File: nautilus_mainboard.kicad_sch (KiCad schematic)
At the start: 0 parts

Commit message: added piezzo circuit and i2c line
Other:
- sheet STM ports: added Pack1_SCL, Pack1_SDA; removed none
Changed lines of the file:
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@@
+	(wire
+		(pts
+			(xy 184.15 93.98) (xy 184.15 90.17)
+		)
+		(stroke
+			(width 0)
+			(type default)
+		)
+	)
+	(wire
+		(pts
+			(xy 184.15 90.17) (xy 55.88 90.17)
+		)
+		(stroke
+			(width 0)
+			(type default)
+		)
+	)
 	(wire
 		(pts
@@
 	(wire
 		(pts
+			(xy 186.69 87.63) (xy 59.69 87.63)
+		)
+		(stroke
+			(width 0)
+			(type default)
+		)
+	)
+	(wire
+		(pts
+			(xy 59.69 87.63) (xy 59.69 76.2)
+		)
+		(stroke
+			(width 0)
+			(type default)
+		)
+	)
+	(wire
+		(pts
+			(xy 186.69 93.98) (xy 186.69 87.63)
+		)
+		(stroke
+			(width 0)
+			(type default)
+		)
+	)
+	(wire
+		(pts
 			(xy 137.16 76.2) (xy 137.16 92.71)
+		)
+		(stroke
+			(width 0)
+			(type default)
+		)
+	)
+	(wire
+		(pts
+			(xy 55.88 90.17) (xy 55.88 76.2)
 		)
 		(stroke
@@
 			)
 		)
+		(pin "Pack1_SCL" input
+			(at 55.88 76.2 270)
+			(effects
+				(font
+					(size 1.27 1.27)
+				)
+				(justify left)
+			)
+		)
+		(pin "Pack1_SDA" input
+			(at 59.69 76.2 270)
+			(effects
+				(font
+					(size 1.27 1.27)
+				)
+				(justify left)
+			)
+		)

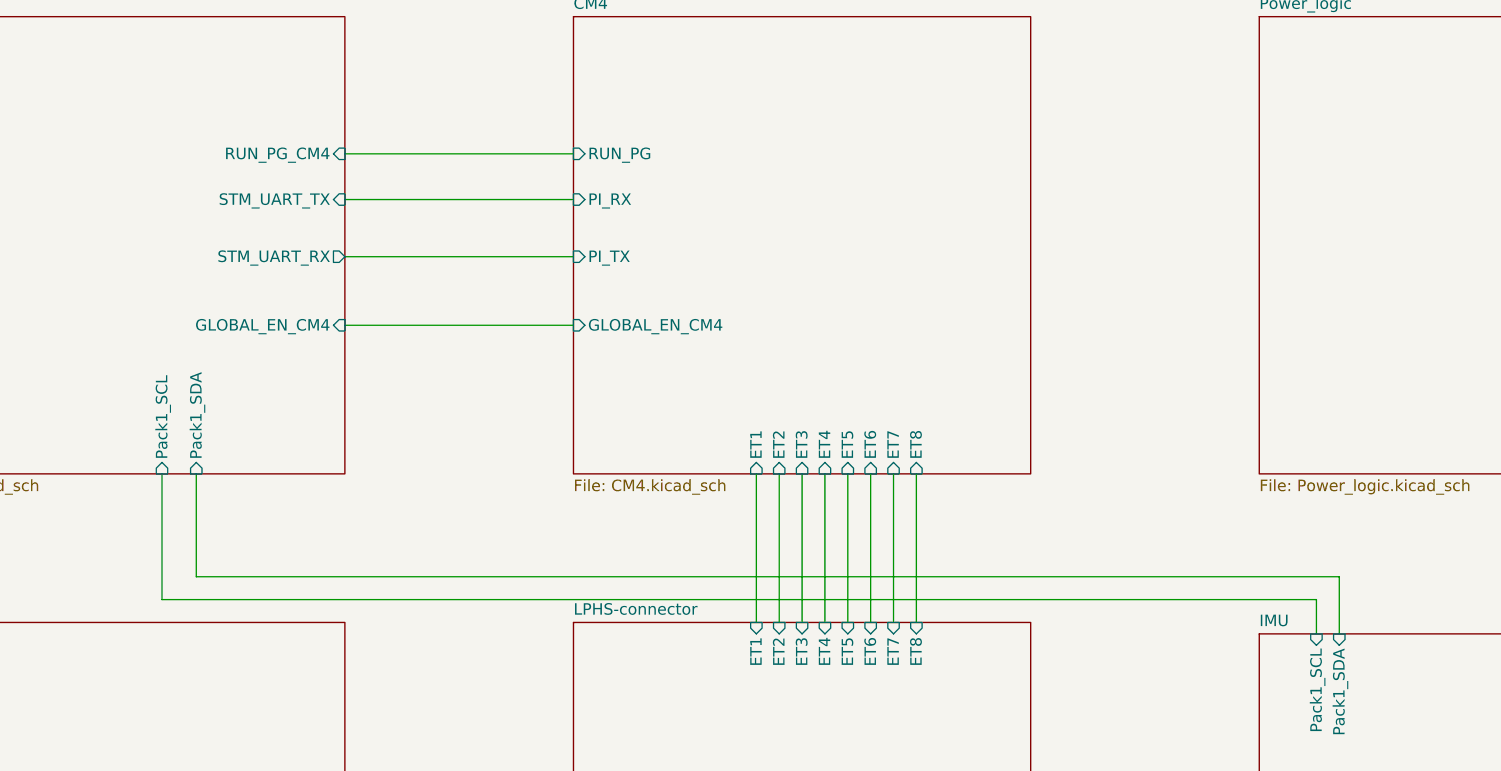
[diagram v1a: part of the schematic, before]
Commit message: added some testpoints
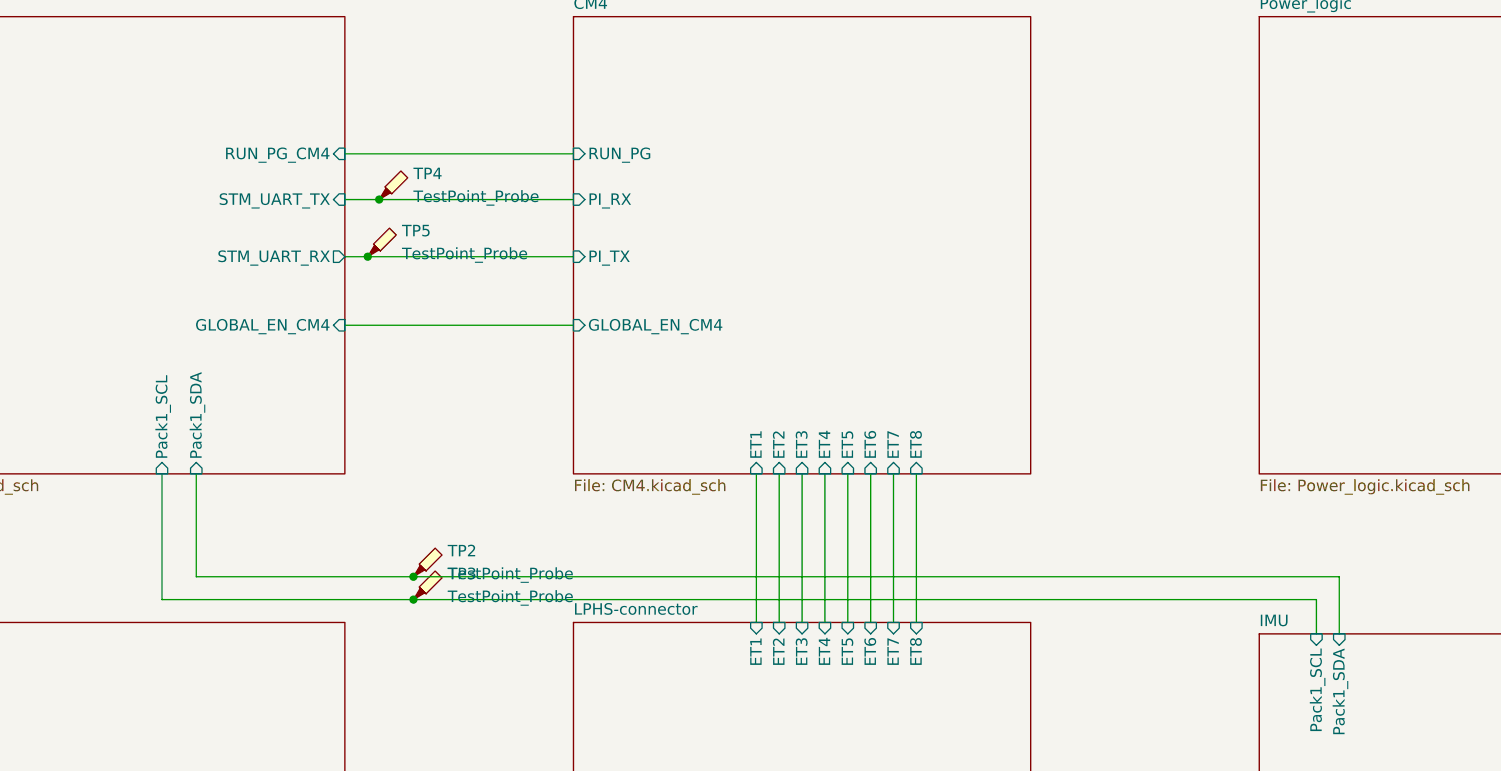
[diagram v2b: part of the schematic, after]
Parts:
- added TP2, TP3: TestPoint_Probe, TestPoint:TestPoint_THTPad_D2.5mm_Drill1.2mm, symbol Connector:TestPoint_Probe
- added TP4, TP5: TestPoint_Probe, TestPoint:TestPoint_Pad_D1.0mm, symbol Connector:TestPoint_Probe
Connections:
- net CM4/PI_RX: now also TP4.1
- net CM4/PI_TX: now also TP5.1
- net IMU/Pack1_SCL: now also TP3.1
- net IMU/Pack1_SDA: now also TP2.1

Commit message: added lan bus
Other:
- sheet CM4 ports: added TRD0{D+ D-}, TRD1{D+ D-}, TRD2{D+ D-}, TRD3{D+ D-}; removed ET1, ET2, ET3, ET4, ET5, ET6, ET7, ET8
- sheet LPHS-connector ports: added TRD0{D+ D-}, TRD1{D+ D-}, TRD2{D+ D-}, TRD3{D+ D-}; removed ET1, ET2, ET3, ET4, ET5, ET6, ET7, ET8

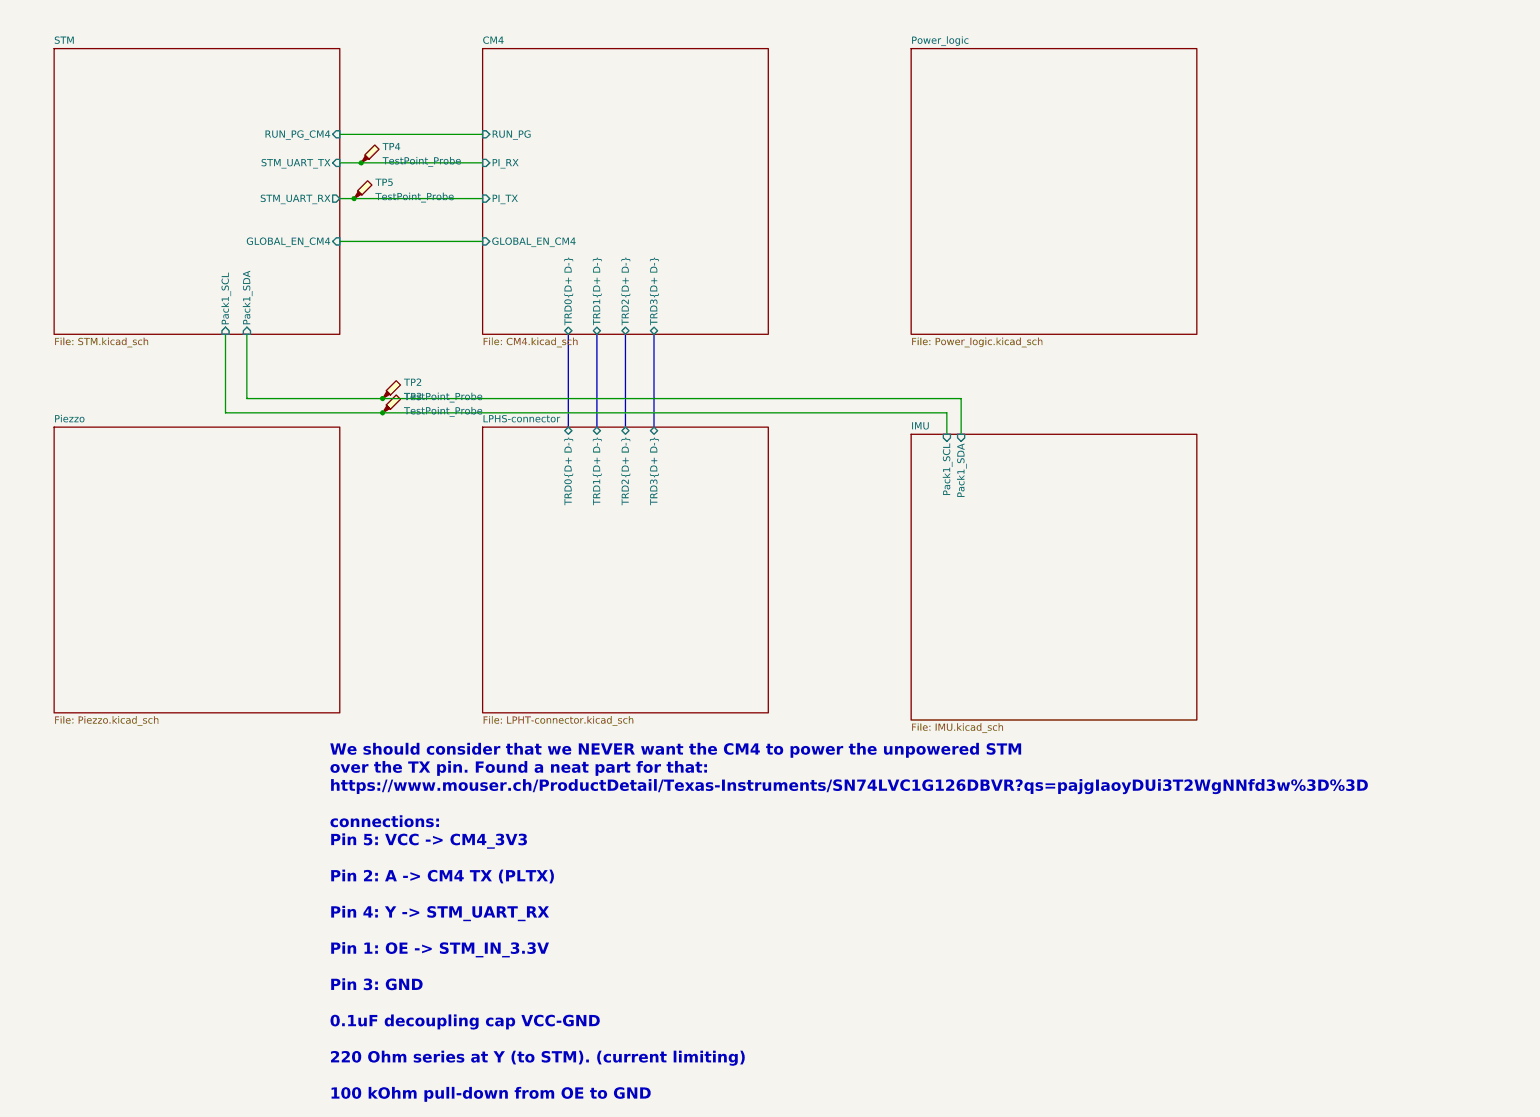
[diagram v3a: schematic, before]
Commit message: chore: multiple cosmetic wiring changes
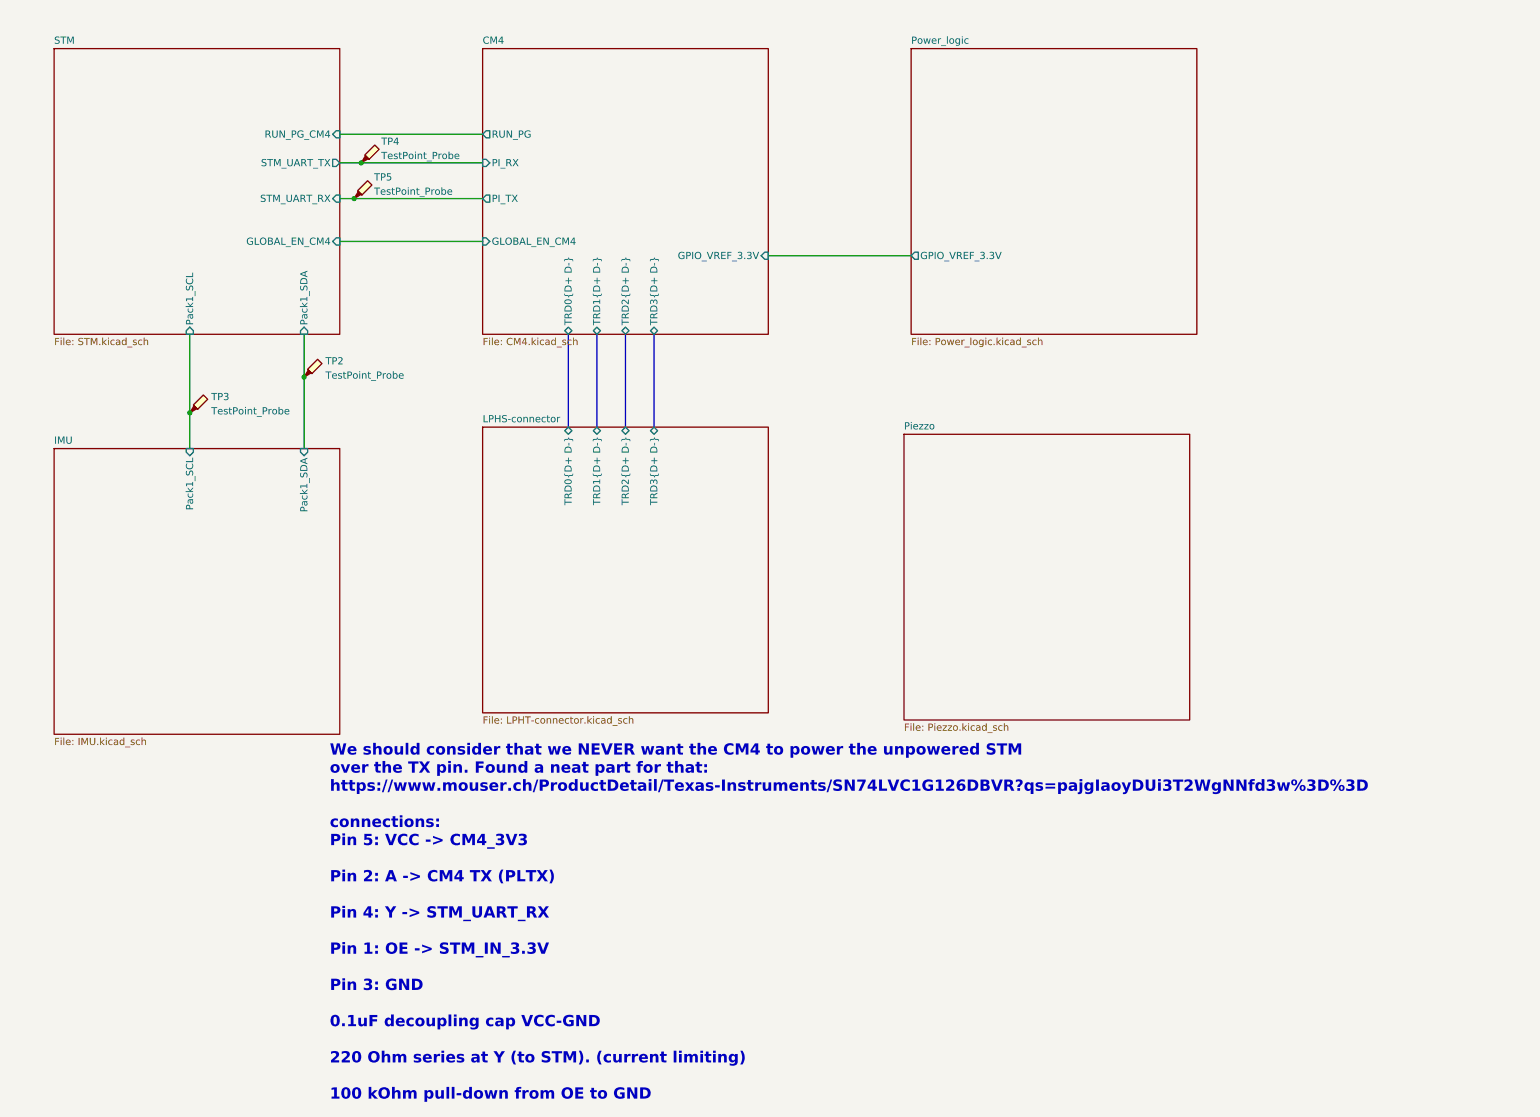
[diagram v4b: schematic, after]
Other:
- sheet CM4 ports: added GPIO_VREF_3.3V; removed none
- sheet Power_logic ports: added GPIO_VREF_3.3V; removed none
- moved on the sheet: TP2, TP3
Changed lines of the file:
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@@
 	)
 	(junction
-		(at 83.82 90.17)
+		(at 49.53 90.17)
 		(diameter 0)
 		(color 0 0 0 0)
 	)
 	(junction
-		(at 83.82 87.63)
+		(at 69.85 83.82)
 		(diameter 0)
 		(color 0 0 0 0)
@@
 	(wire
 		(pts
+			(xy 69.85 83.82) (xy 69.85 76.2)
+		)
+		(stroke
+			(width 0)
+			(type default)
+		)
+	)
+	(wire
+		(pts
 			(xy 76.2 52.07) (xy 78.74 52.07)
 		)
@@
 	(wire
 		(pts
-			(xy 184.15 93.98) (xy 184.15 90.17)
+			(xy 49.53 96.52) (xy 49.53 90.17)
 		)
 		(stroke
@@
 	(wire
 		(pts
-			(xy 55.88 90.17) (xy 83.82 90.17)
-		)
-		(stroke
-			(width 0)
-			(type default)
-		)
-	)
-	(wire
-		(pts
 			(xy 76.2 59.69) (xy 101.6 59.69)
 		)
@@
 	(wire
 		(pts
-			(xy 186.69 87.63) (xy 83.82 87.63)
-		)
-		(stroke
-			(width 0)
-			(type default)
-		)
-	)
-	(wire
-		(pts
-			(xy 83.82 90.17) (xy 184.15 90.17)
-		)
-		(stroke
-			(width 0)
-			(type default)
-		)
-	)
-	(wire
-		(pts
-			(xy 59.69 87.63) (xy 59.69 76.2)
-		)
-		(stroke
-			(width 0)
-			(type default)
-		)
-	)
-	(wire
-		(pts
-			(xy 83.82 87.63) (xy 59.69 87.63)
-		)
-		(stroke
-			(width 0)
-			(type default)
-		)
-	)
-	(wire
-		(pts
-			(xy 186.69 93.98) (xy 186.69 87.63)
+			(xy 152.4 62.23) (xy 177.8 62.23)
 		)
 		(stroke
@@
 	(wire
 		(pts
-			(xy 55.88 90.17) (xy 55.88 76.2)
+			(xy 69.85 83.82) (xy 69.85 96.52)
+		)
+		(stroke
+			(width 0)
+			(type default)
+		)
+	)
+	(wire
+		(pts
+			(xy 49.53 90.17) (xy 49.53 76.2)
 		)
 		(stroke
@@
 		(on_board yes)
 		(dnp no)
-		(fields_autoplaced yes)
 		(property "Reference" "TP4"
-			(at 83.82 42.8624 0)
+			(at 83.566 41.91 0)
 			(effects
 				(font
@@
 		)
 		(property "Value" "TestPoint_Probe"
-			(at 83.82 45.4024 0)
+			(at 83.566 44.45 0)
 			(effects
 				(font
@@
 	(symbol
 		(lib_id "Connector:TestPoint_Probe")
-		(at 83.82 87.63 0)
+		(at 69.85 83.82 0)
 		(unit 1)
 		(exclude_from_sim no)
@@
 		(fields_autoplaced yes)
 		(property "Reference" "TP2"
-			(at 87.63 84.7724 0)
+			(at 73.66 80.9624 0)
 			(effects
 				(font
@@
 		)
 		(property "Value" "TestPoint_Probe"
-			(at 87.63 87.3124 0)
+			(at 73.66 83.5024 0)
 			(effects
 				(font
@@
 		)
 		(property "Footprint" "TestPoint:TestPoint_THTPad_D2.5mm_Drill1.2mm"
-			(at 88.9 87.63 0)
+			(at 74.93 83.82 0)
 			(effects
 				(font
@@
 		)
 		(property "Datasheet" "~"
-			(at 88.9 87.63 0)
+			(at 74.93 83.82 0)
 			(effects
 				(font
@@
 		)
 		(property "Description" "test point (alternative probe-style design)"
-			(at 83.82 87.63 0)
+			(at 69.85 83.82 0)
 			(effects
 				(font
@@
 	(symbol
 		(lib_id "Connector:TestPoint_Probe")
-		(at 83.82 90.17 0)
+		(at 49.53 90.17 0)
 		(unit 1)
 		(exclude_from_sim no)
@@
 		(fields_autoplaced yes)
 		(property "Reference" "TP3"
-			(at 87.63 87.3124 0)
+			(at 53.34 87.3124 0)
 			(effects
 				(font
@@
 		)
 		(property "Value" "TestPoint_Probe"
-			(at 87.63 89.8524 0)
+			(at 53.34 89.8524 0)
 			(effects
 				(font
@@
 		)
 		(property "Footprint" "TestPoint:TestPoint_THTPad_D2.5mm_Drill1.2mm"
-			(at 88.9 90.17 0)
+			(at 54.61 90.17 0)
 			(effects
 				(font
@@
 		)
 		(property "Datasheet" "~"
-			(at 88.9 90.17 0)
+			(at 54.61 90.17 0)
 			(effects
 				(font
@@
 		)
 		(property "Description" "test point (alternative probe-style design)"
-			(at 83.82 90.17 0)
+			(at 49.53 90.17 0)
 			(effects
 				(font
@@
 		(on_board yes)
 		(dnp no)
-		(fields_autoplaced yes)
 		(property "Reference" "TP5"
-			(at 82.55 49.2124 0)
+			(at 82.296 48.26 0)
 			(effects
 				(font
@@
 		)
 		(property "Value" "TestPoint_Probe"
-			(at 82.55 51.7524 0)
+			(at 82.296 50.8 0)
 			(effects
 				(font
@@
 			)
 		)
-		(pin "STM_UART_RX" output
-			(at 76.2 52.07 0)
-			(effects
-				(font
-					(size 1.27 1.27)
-				)
-				(justify right)
-			)
-		)
-		(pin "STM_UART_TX" input
-			(at 76.2 45.72 0)
-			(effects
-				(font
-					(size 1.27 1.27)
-				)
-				(justify right)
-			)
-		)
 		(pin "RUN_PG_CM4" input
 			(at 76.2 40.64 0)
@@
 		)
 		(pin "Pack1_SCL" input
-			(at 55.88 76.2 270)
+			(at 49.53 76.2 270)
 			(effects
 				(font
@@
 		)
 		(pin "Pack1_SDA" input
-			(at 59.69 76.2 270)
-			(effects
-				(font
-					(size 1.27 1.27)
-				)
-				(justify left)
+			(at 69.85 76.2 270)
+			(effects
+				(font
+					(size 1.27 1.27)
+				)
+				(justify left)
+			)
+		)
+		(pin "STM_UART_RX" input
+			(at 76.2 52.07 0)
+			(effects
+				(font
+					(size 1.27 1.27)
+				)
+				(justify right)
+			)
+		)
+		(pin "STM_UART_TX" output
+			(at 76.2 45.72 0)
+			(effects
+				(font
+					(size 1.27 1.27)
+				)
+				(justify right)
 			)
 		)
@@
 	)
 	(sheet
-		(at 25.4 92.71)
+		(at 176.53 93.98)
 		(size 50.8 50.8)
 		(exclude_from_sim no)
@@
 		)
 		(property "Sheetname" "Piezzo"
-			(at 25.4 91.9984 0)
+			(at 176.53 93.2684 0)
 			(effects
 				(font
@@
 		)
 		(property "Sheetfile" "Piezzo.kicad_sch"
-			(at 25.4 144.0946 0)
+			(at 176.53 145.3646 0)
 			(effects
 				(font
@@
 	)
 	(sheet
-		(at 177.8 93.98)
+		(at 25.4 96.52)
 		(size 50.8 50.8)
 		(exclude_from_sim no)
@@
 		)
 		(property "Sheetname" "IMU"
-			(at 177.8 93.2684 0)
+			(at 25.4 95.8084 0)
 			(effects
 				(font
@@
 		)
 		(property "Sheetfile" "IMU.kicad_sch"
-			(at 177.8 145.3646 0)
+			(at 25.4 147.9046 0)
 			(effects
 				(font
@@
 		)
 		(pin "Pack1_SCL" input
-			(at 184.15 93.98 90)
+			(at 49.53 96.52 90)
 			(effects
 				(font
@@
 		)
 		(pin "Pack1_SDA" input
-			(at 186.69 93.98 90)
+			(at 69.85 96.52 90)
 			(effects
 				(font
@@
 			)
 		)
+		(pin "GPIO_VREF_3.3V" output
+			(at 177.8 62.23 180)
+			(effects
+				(font
+					(size 1.27 1.27)
+				)
+				(justify left)
+			)
+		)
 		(instances
 			(project "nautilus_mainboard"
@@
 			)
 		)
-		(pin "PI_TX" input
+		(pin "PI_TX" output
 			(at 101.6 52.07 180)
 			(effects
@@
 			)
 		)
-		(pin "RUN_PG" input
+		(pin "RUN_PG" output
 			(at 101.6 40.64 180)
 			(effects
@@
 			)
 		)
+		(pin "GPIO_VREF_3.3V" input
+			(at 152.4 62.23 0)
+			(effects
+				(font
+					(size 1.27 1.27)
+				)
+				(justify right)
+			)
+		)

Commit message: chore: Many routing changes
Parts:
- added TP1, TP8, TP9: TestPoint_Probe, TestPoint:TestPoint_Pad_D1.0mm, symbol Connector:TestPoint_Probe
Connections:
- new net CM4/Battery_Out_3.3V: TP8.1
- new net GND: TP9.1
- new net LPHS-connector/Battery_Out_5V: TP1.1
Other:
- sheet CM4 ports: added Battery_Out_3.3V, CM4_Out_3.3V, LAN_IN_3.3V, USB_Out_5V; removed none
- sheet LPHS-connector ports: added Battery_Out_3.3V, Battery_Out_5V; removed none
- sheet Piezzo ports: added Piezo_ctrl; removed none
- sheet Power_logic ports: added Battery_Out_3.3V, Battery_Out_5V, CM4_Out_3.3V, LAN_IN_3.3V, STM_Plug_3.3V, USB_Out_5V; removed none
- sheet STM ports: added Battery_Out_3.3V, STM_Plug_3.3V; removed none
- note added: "Standard 5V and 3.3V for the components are sent out as globals."
- moved on the sheet: TP2, TP3, TP4, TP5
